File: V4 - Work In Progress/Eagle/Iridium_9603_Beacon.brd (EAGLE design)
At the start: 57.6 x 66 mm, 77 parts, among them CON4 uFL, J1 SS4-10-3.50-X-D, Q1 DMG3415U-7, U1 MCP111T-240E/TT, U2 SPX3819-3.3, U3 LTC3225EDDB#TRMPBF, U4 MPL3115A2LGA8, U5 ATSAMD21G18_QFN, U6 MAX-M8, U7 LT1634-1,25BMCMS8, X1 32.768

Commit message: Minor updates
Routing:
- net VBUS: track 155.1 -> 153.1 mm
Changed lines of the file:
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@@
 <?xml version="1.0" encoding="utf-8"?>
 <!DOCTYPE eagle SYSTEM "eagle.dtd">
-<eagle version="8.5.0">
+<eagle version="8.6.0">
 <drawing>
 <settings>
@@
 <wire x1="15.8115" y1="25.4" x2="15.8115" y2="27.27325" width="0.6096" layer="1"/>
 <wire x1="16.4799" y1="23.21175" x2="14.57075" y2="23.21175" width="0.4064" layer="1"/>
-<wire x1="31.5595" y1="16.1925" x2="35.52825" y2="20.16125" width="0.8128" layer="16"/>
-<wire x1="31.5595" y1="16.1925" x2="31.5595" y2="14.732" width="0.8128" layer="16"/>
 <wire x1="38.5445" y1="43.96105" x2="38.5445" y2="44.35475" width="0.2032" layer="1"/>
 <wire x1="38.5445" y1="44.35475" x2="37.7825" y2="45.11675" width="0.2032" layer="1"/>
@@
 <wire x1="25.24125" y1="53.11775" x2="25.4" y2="52.959" width="0.8128" layer="1"/>
 <wire x1="20.54225" y1="25.527" x2="20.54225" y2="16.28775" width="0.8128" layer="16"/>
-<wire x1="20.54225" y1="16.28775" x2="22.098" y2="14.732" width="0.8128" layer="16"/>
-<wire x1="22.098" y1="14.732" x2="31.5595" y2="14.732" width="0.8128" layer="16"/>
 <wire x1="37.7825" y1="52.7685" x2="37.81425" y2="52.80025" width="0.8128" layer="16"/>
 <wire x1="37.81425" y1="52.80025" x2="37.6555" y2="52.959" width="0.8128" layer="16"/>
@@
 <wire x1="35.1155" y1="14.312" x2="35.1155" y2="15.14475" width="0.4064" layer="1"/>
 <via x="35.1155" y="15.14475" extent="1-16" drill="0.254" diameter="0.8128"/>
-<wire x1="35.1155" y1="15.14475" x2="31.97225" y2="15.14475" width="0.6096" layer="16"/>
-<wire x1="31.97225" y1="15.14475" x2="31.90875" y2="15.08125" width="0.4064" layer="16"/>
-<wire x1="31.90875" y1="15.08125" x2="31.5595" y2="14.732" width="0.4064" layer="16"/>
 <wire x1="12.98325" y1="23.39975" x2="14.38275" y2="23.39975" width="0.6096" layer="1"/>
 <wire x1="14.38275" y1="23.39975" x2="14.50975" y2="23.27275" width="0.6096" layer="1"/>
@@
 <wire x1="31.496" y1="11.0575" x2="31.496" y2="12.319" width="0.4064" layer="1"/>
 <via x="31.496" y="12.319" extent="1-16" drill="0.254" diameter="0.6096"/>
-<wire x1="31.496" y1="12.319" x2="31.90875" y2="12.73175" width="0.4064" layer="16"/>
-<wire x1="31.90875" y1="12.73175" x2="31.90875" y2="15.08125" width="0.4064" layer="16"/>
+<wire x1="20.54225" y1="16.28775" x2="21.68525" y2="15.14475" width="0.8128" layer="16"/>
+<wire x1="21.68525" y1="15.14475" x2="31.75" y2="15.14475" width="0.8128" layer="16"/>
+<wire x1="31.75" y1="15.14475" x2="35.1155" y2="15.14475" width="0.8128" layer="16"/>
+<wire x1="31.9512" y1="13.64961875" x2="31.75" y2="13.85081875" width="0.8128" layer="16"/>
+<wire x1="31.75" y1="13.85081875" x2="31.75" y2="15.14475" width="0.8128" layer="16"/>
+<wire x1="31.496" y1="12.319" x2="31.9512" y2="12.7742" width="0.8128" layer="16"/>
+<wire x1="31.9512" y1="12.7742" x2="31.9512" y2="13.64961875" width="0.8128" layer="16"/>
+<wire x1="35.52825" y1="20.16393125" x2="35.1155" y2="19.75118125" width="0.8128" layer="16"/>
+<wire x1="35.1155" y1="19.75118125" x2="35.1155" y2="15.14475" width="0.8128" layer="16"/>
 </signal>
 <signal name="GND">

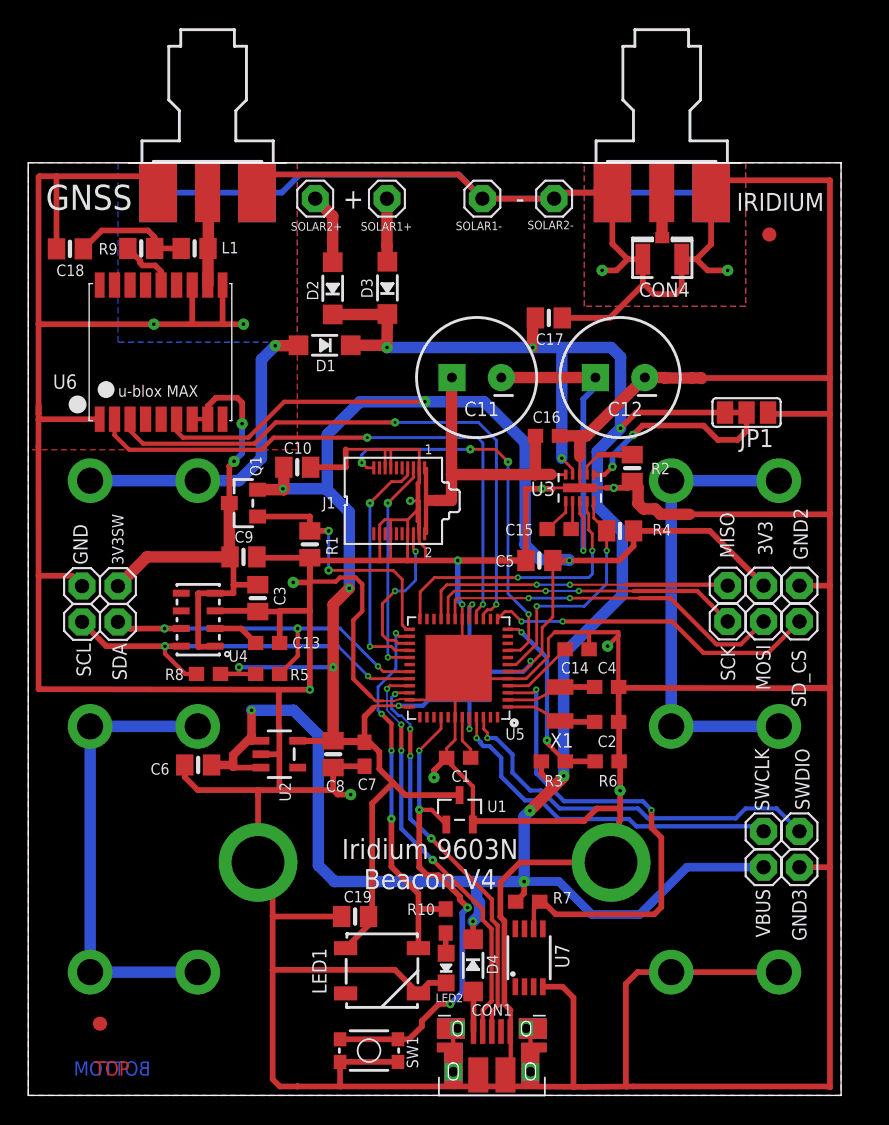
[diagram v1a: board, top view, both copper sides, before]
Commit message: Added split pads for supercapacitor charge current
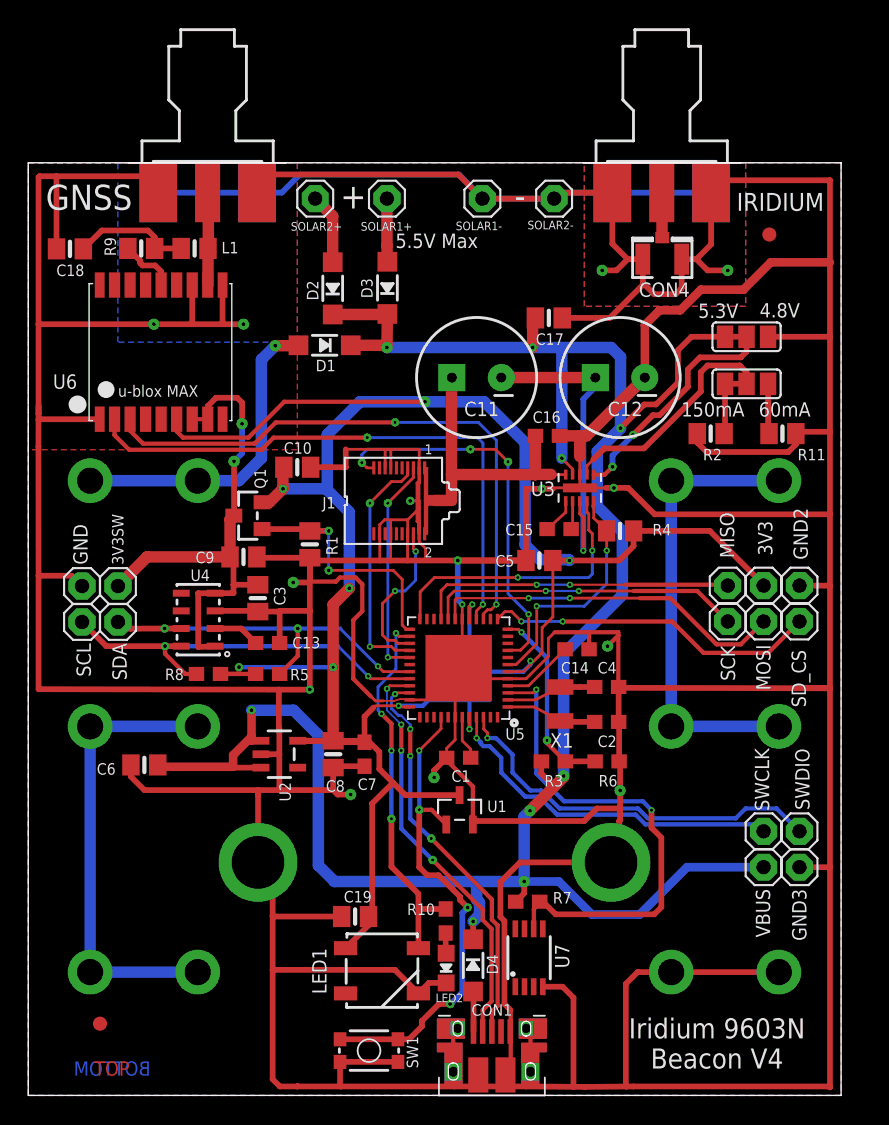
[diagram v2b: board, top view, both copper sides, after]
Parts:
- added JP2: (no value), SparkFun-Passives:PAD-JUMPER-3-2OF3_NC_BY_TRACE_YES_SILK_LARGE
- added R11: 30K, microbuilder:0805-NO
- R2: value 30K -> 12K
- moved R2 6.07 mm to (48.3, 46.9), turned to 0 degrees
- moved JP1 5.37 mm to (50.9, 53.7)
- moved C6 3.81 mm to (8.22, 23.4)
- moved Q1 0.94 mm to (15.6, 41.1)
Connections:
- new net N$17: JP2.3, R2.2
- new net N$18: JP2.1, R11.2
- net GND: now also R11.1
- net N$11: now also JP2.2; no longer R2.2
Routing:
- net GND: track 691.4 -> 710.1 mm
- net N$11: track 4.45 -> 16.7 mm
- net VBUS: track 153.1 -> 160.3 mm
- net N$17: track 0.00 -> 3.55 mm
- net N$18: track 0.00 -> 3.55 mm
- net N$13: track 14.7 -> 16.7 mm
- net D11: track 18.2 -> 16.9 mm
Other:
- board text added: "150mA"
- board text added: "4.8V"
- board text added: "5.3V"
- board text added: "5.5V Max"
- board text added: "60mA"

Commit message: Minor tweaks
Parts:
- moved C6 10.7 mm to (18.2, 27.3), turned to 0 degrees
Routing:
- net GND: track 710.1 -> 700.3 mm
- net VBUS: track 160.3 -> 156.2 mm
- net MISO: track 22.5 -> 23.1 mm
